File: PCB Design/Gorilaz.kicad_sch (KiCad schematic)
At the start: 44 parts, among them J1 Conn_01x13, J2 Conn_01x13, J3 Conn_01x13, J4 Conn_01x13, J5 Conn_01x13, J6 Conn_01x13, J7 Battery, J8 HRO_TYPE-C-31-M-14, SW1 SW_DPST_x2, SW4 RST, U1 SRV05-4, U10 MAX17048, U3 BQ24075, U4 DW01A, U5 FS8205, U8 nRF52840_moko_mk08

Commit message: up
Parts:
- J7: footprint Local:Molex_Pico-EZmate_78171-0002_1x02-1MP_P1.20mm_Vertical -> Connector_JST:JST_GH_BM02B-GHS-TBT_1x02-1MP_P1.25mm_Vertical
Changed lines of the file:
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@@
 			)
 		)
-		(property "Footprint" "Local:Molex_Pico-EZmate_78171-0002_1x02-1MP_P1.20mm_Vertical"
+		(property "Footprint" "Connector_JST:JST_GH_BM02B-GHS-TBT_1x02-1MP_P1.25mm_Vertical"
 			(at 215.9 52.07 0)
 			(effects

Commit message: update pre-prod
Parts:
- removed SW1: SW_DPST_x2, symbol Switch:SW_DPST_x2
- added JP1: power on, symbol Jumper:SolderJumper_2_Open
- D1, D2, D3: footprint LED_SMD:LED_1206_3216Metric -> LED_SMD:LED_1206_3216Metric_ReverseMount_Hole1.8x2.4mm
- J2: footprint Molex_0039532135 -> Local:Molex_0039532135
- J7: footprint Connector_JST:JST_GH_BM02B-GHS-TBT_1x02-1MP_P1.25mm_Vertical -> Connector_JST:JST_PH_B2B-PH-K_1x02_P2.00mm_Vertical
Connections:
- net +BATT: now also JP1.2 (B)
- net at J7.1 (Pin_1): now also JP1.1 (A)
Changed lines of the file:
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@@
 	(wire
 		(pts
-			(xy 231.14 52.07) (xy 233.68 52.07)
+			(xy 228.6 52.07) (xy 233.68 52.07)
 		)
 		(stroke
@@
 			)
 		)
-		(property "Footprint" "Molex_0039532135"
+		(property "Footprint" "Local:Molex_0039532135"
 			(at 50.8 93.98 0)
 			(effects
@@
 			)
 		)
-		(property "Footprint" "LED_SMD:LED_1206_3216Metric"
+		(property "Footprint" "LED_SMD:LED_1206_3216Metric_ReverseMount_Hole1.8x2.4mm"
 			(at 240.03 180.34 0)
 			(effects
@@
 			)
 		)
-		(property "Footprint" "LED_SMD:LED_1206_3216Metric"
+		(property "Footprint" "LED_SMD:LED_1206_3216Metric_ReverseMount_Hole1.8x2.4mm"
 			(at 281.94 179.07 0)
 			(effects
@@
 	)
 	(symbol
+		(lib_id "Jumper:SolderJumper_2_Open")
+		(at 224.79 52.07 0)
+		(unit 1)
+		(exclude_from_sim no)
+		(in_bom no)
+		(on_board yes)
+		(dnp no)
+		(fields_autoplaced yes)
+		(property "Reference" "JP1"
+			(at 224.79 45.72 0)
+			(effects
+				(font
+					(size 1.27 1.27)
+				)
+			)
+		)
+		(property "Value" "power on"
+			(at 224.79 48.26 0)
+			(effects
+				(font
+					(size 1.27 1.27)
+				)
+			)
+		)
+		(property "Footprint" ""
+			(at 224.79 52.07 0)
+			(effects
+				(font
+					(size 1.27 1.27)
+				)
+				(hide yes)
+			)
+		)
+		(property "Datasheet" "~"
+			(at 224.79 52.07 0)
+			(effects
+				(font
+					(size 1.27 1.27)
+				)
+				(hide yes)
+			)
+		)
+		(property "Description" "Solder Jumper, 2-pole, open"
+			(at 224.79 52.07 0)
+			(effects
+				(font
+					(size 1.27 1.27)
+				)
+				(hide yes)
+			)
+		)
+		(pin "1"
+		)
+		(pin "2"
+		)
+		(instances
+			(project ""
+				(path "/46ef0abf-42df-44ff-8272-0b82956755c4"
+					(reference "JP1")
+					(unit 1)
+				)
+			)
+		)
+	)
+	(symbol
 		(lib_id "power:GND")
 		(at 124.46 66.04 0)
@@
 			)
 		)
-		(property "Footprint" "LED_SMD:LED_1206_3216Metric"
+		(property "Footprint" "LED_SMD:LED_1206_3216Metric_ReverseMount_Hole1.8x2.4mm"
 			(at 269.24 179.07 0)
 			(effects
@@
 	)
 	(symbol
-		(lib_id "Switch:SW_DPST_x2")
-		(at 226.06 52.07 0)
-		(unit 1)
-		(exclude_from_sim no)
-		(in_bom yes)
-		(on_board yes)
-		(dnp no)
-		(fields_autoplaced yes)
-		(property "Reference" "SW1"
-			(at 226.06 45.72 0)
-			(effects
-				(font
-					(size 1.27 1.27)
-				)
-			)
-		)
-		(property "Value" "SW_DPST_x2"
-			(at 226.06 48.26 0)
-			(effects
-				(font
-					(size 1.27 1.27)
-				)
-			)
-		)
-		(property "Footprint" ""
-			(at 226.06 52.07 0)
-			(effects
-				(font
-					(size 1.27 1.27)
-				)
-				(hide yes)
-			)
-		)
-		(property "Datasheet" "~"
-			(at 226.06 52.07 0)
-			(effects
-				(font
-					(size 1.27 1.27)
-				)
-				(hide yes)
-			)
-		)
-		(property "Description" "Single Pole Single Throw (SPST) switch, separate symbol"
-			(at 226.06 52.07 0)
-			(effects
-				(font
-					(size 1.27 1.27)
-				)
-				(hide yes)
-			)
-		)
-		(pin "3"
-		)
-		(pin "2"
-		)
-		(pin "1"
-		)
-		(pin "4"
-		)
-		(instances
-			(project ""
-				(path "/46ef0abf-42df-44ff-8272-0b82956755c4"
-					(reference "SW1")
-					(unit 1)
-				)
-			)
-		)
-	)
-	(symbol
 		(lib_id "power:+BATT")
 		(at 285.75 58.42 0)
@@
 			)
 		)
-		(property "Footprint" "Connector_JST:JST_GH_BM02B-GHS-TBT_1x02-1MP_P1.25mm_Vertical"
+		(property "Footprint" "Connector_JST:JST_PH_B2B-PH-K_1x02_P2.00mm_Vertical"
 			(at 215.9 52.07 0)
 			(effects

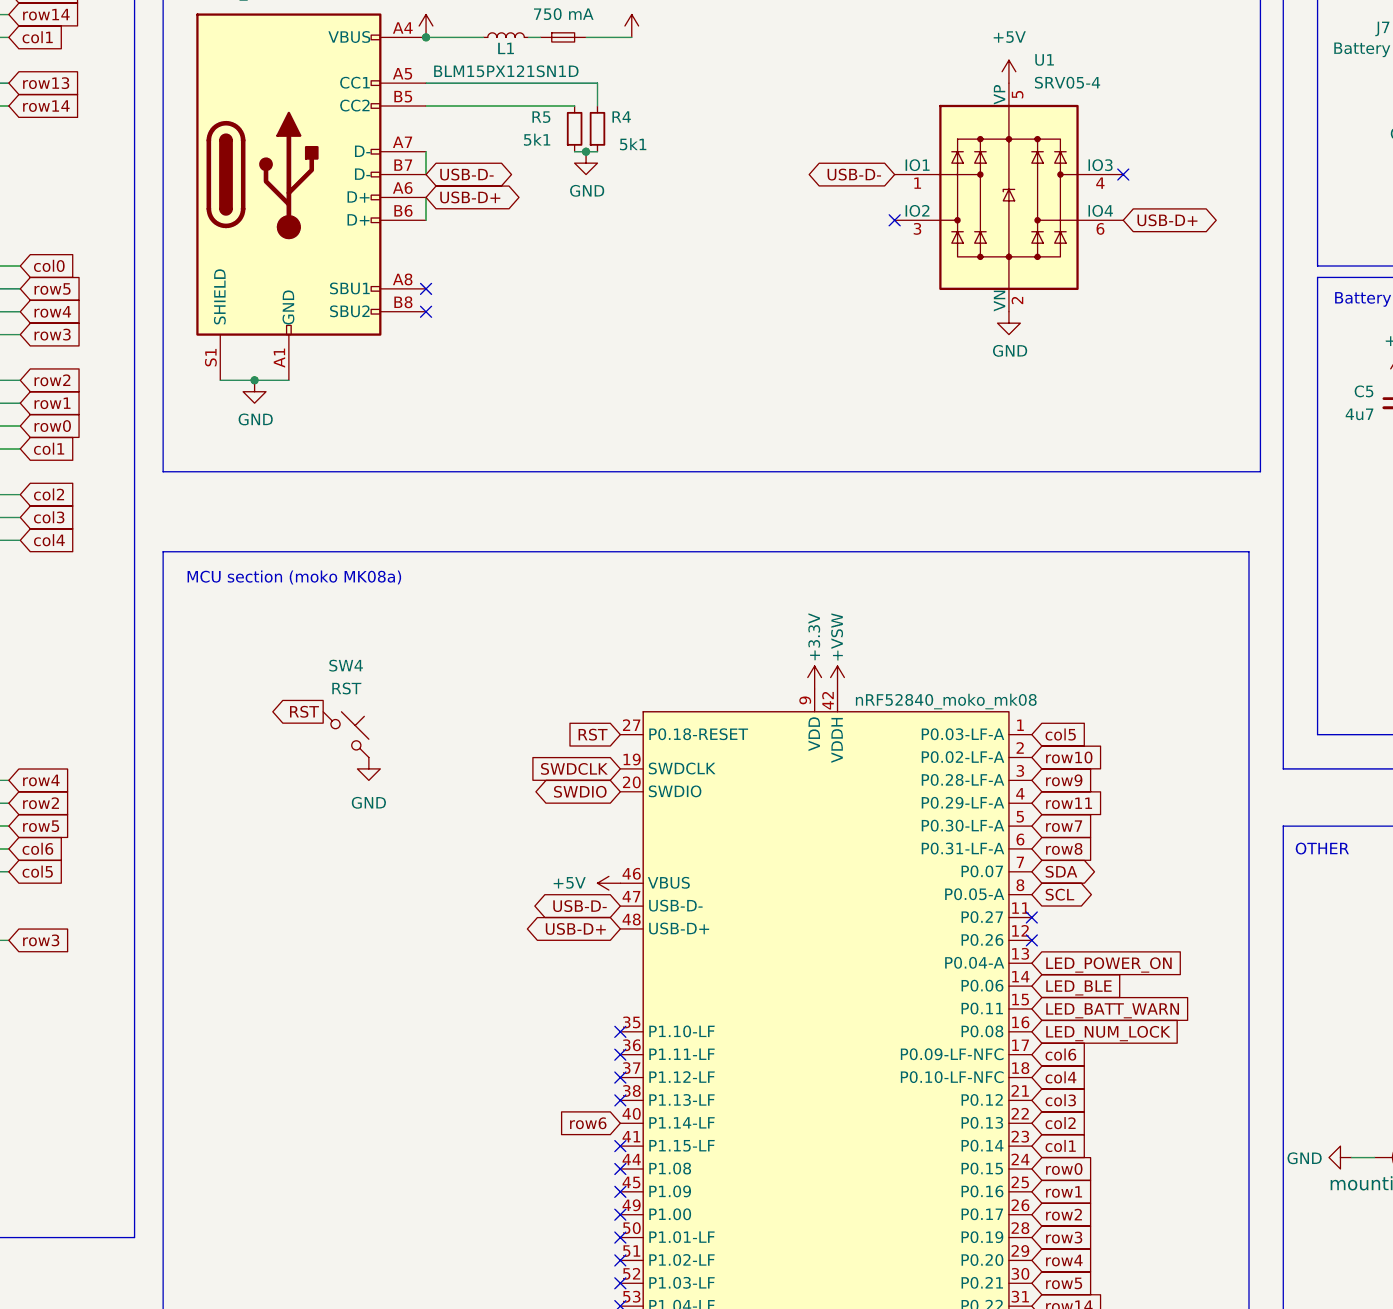
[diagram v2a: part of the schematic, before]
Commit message: ESD update
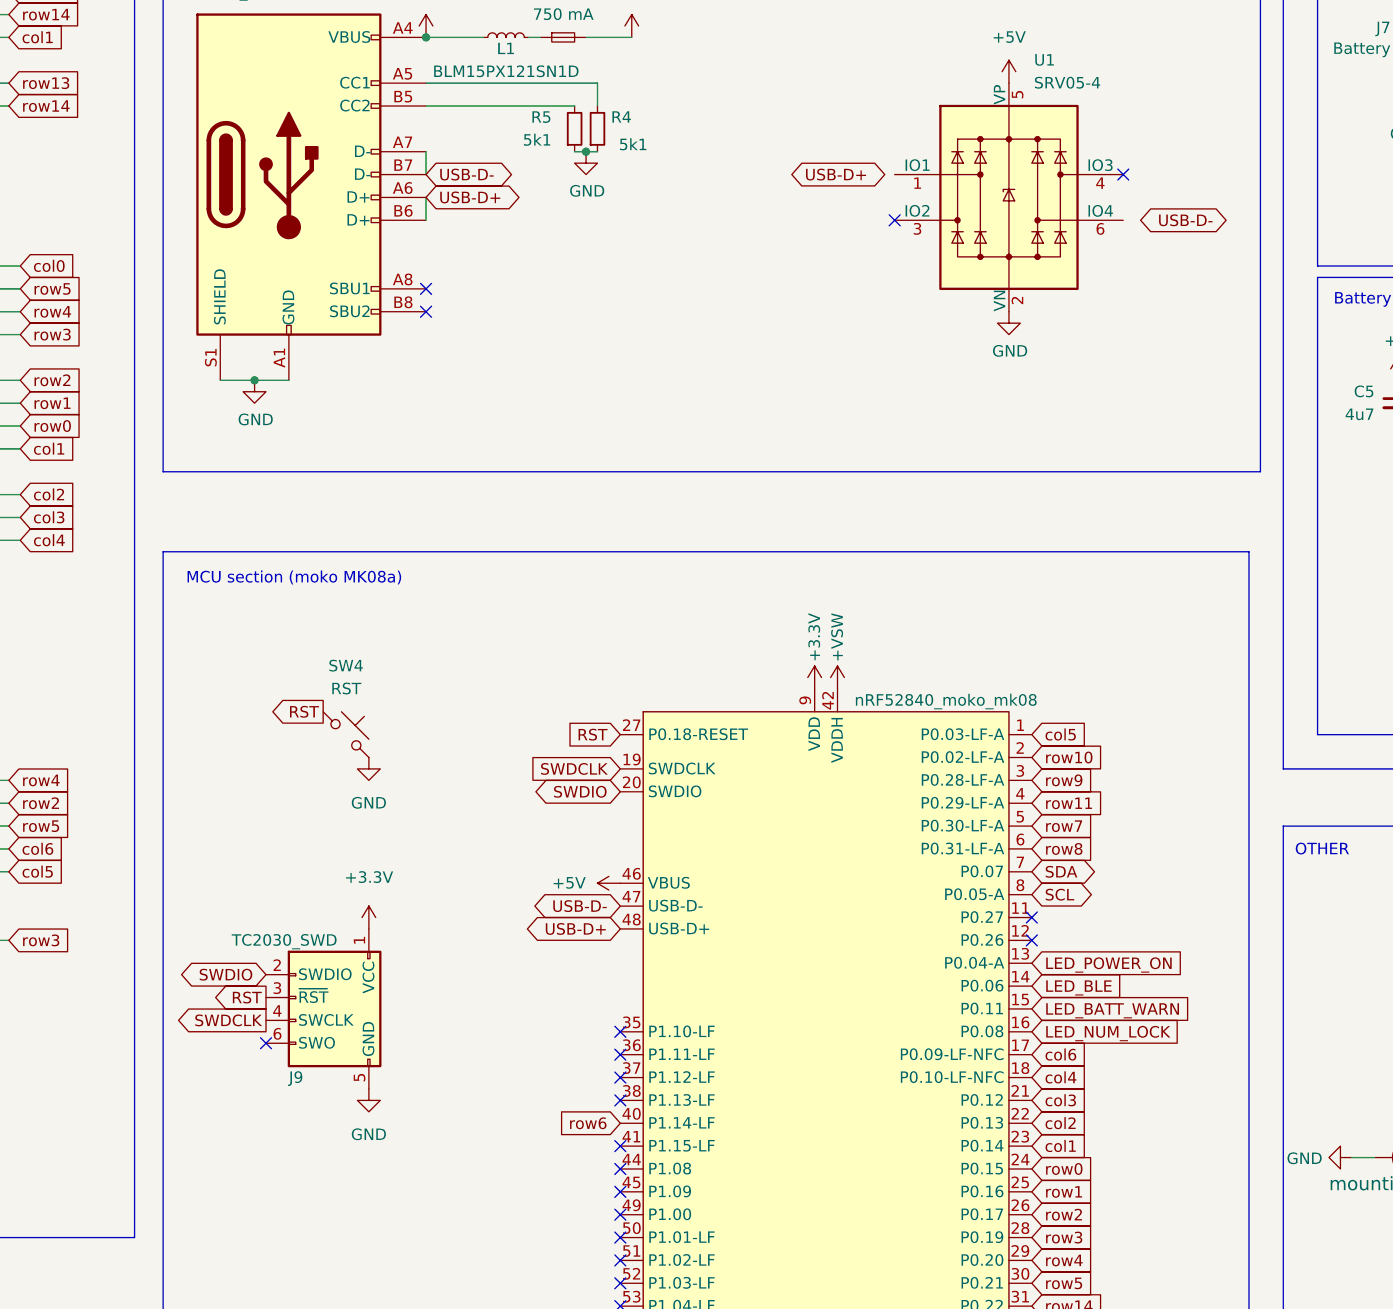
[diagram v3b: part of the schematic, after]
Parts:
- added J9: TC2030_SWD, Mastarlib:CON_TC2030_outlined, symbol PCM_marbastlib-various:TC2030_SWD
- JP1: footprint (none) -> Jumper:SolderJumper-2_P1.3mm_Open_RoundedPad1.0x1.5mm
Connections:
- net +3.3V: now also J9.1 (VCC)
- net GND: now also J9.5 (GND)
- net RST: now also J9.3 (~{RST})
- net SWDCLK: now also J9.4 (SWCLK)
- net SWDIO: now also J9.2 (SWDIO)
- net USB-D+: no longer U1.6 (IO4)
- net USB-D-: no longer U1.1 (IO1)
- no-connect marks 45 -> 46

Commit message: lots of improvement
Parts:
- removed J8: HRO_TYPE-C-31-M-14, Connector_USB:USB_C_Receptacle_HRO_TYPE-C-31-M-12, symbol Connector:USB_C_Receptacle_USB2.0
- removed J9: TC2030_SWD, Mastarlib:CON_TC2030_outlined, symbol PCM_marbastlib-various:TC2030_SWD
- removed JP1: power on, Jumper:SolderJumper-2_P1.3mm_Open_RoundedPad1.0x1.5mm, symbol Jumper:SolderJumper_2_Open
- removed R4, R5: 5k1, Resistor_SMD:R_0402_1005Metric, symbol Device:R_Small
- added C3: 4u7, Capacitor_SMD:C_0402_1005Metric, symbol Device:C_Small
- added CN1: 950-D-SMD-DS/02, easyeda:CONN-SMD_2P-P5.00_950-D-SMD-DS-02, symbol easyea:950-D-SMD-DS_02
- added J8: Conn_01x05_MountingPin, Connector_PinHeader_2.54mm:PinHeader_1x05_P2.54mm_Vertical, symbol Connector_Generic_MountingPin:Conn_01x05_MountingPin
- added R1, R2: 5k1, Resistor_SMD:R_0402_1005Metric, symbol Device:R_Small
- added USB1: USB-310M-B-SU, easyeda:USB-C-SMD_USB-310M-B-SU, symbol easyea:USB-310M-B-SU
- renumbered C8 to C1, C5 to C2, C6 to C4, C17 to C5, LED2 to D1, LED1 to D2, D1 to D3, D2 to D4, D3 to D5, R1 to R10, R2 to R11, R18 to R12, R19 to R13, R20 to R14, R21 to R15, R22 to R16, R15 to R3, R17 to R4, R11 to R5, R12 to R6, R13 to R7, R9 to R8, R10 to R9, SW4 to SW1, U5 to U2, U4 to U3, U3 to U4, U10 to U5
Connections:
- net +3.3V: now also J8.1 (Pin_1)
- net +BATT: now also C3.1, CN1.2
- net ALERT: now also U8.54 (P1.05-LF)
- net GND: now also C3.2, J8.5 (Pin_5), J8.MP (MountPin), R1.1, R2.1, USB1.1 (SHELL), USB1.2 (SHELL), USB1.3 (SHELL), USB1.4 (SHELL), USB1.A1B12 (GND), USB1.B1A12 (GND)
- net RST: now also J8.3 (Pin_3)
- net SWDCLK: now also J8.4 (Pin_4)
- net SWDIO: now also J8.2 (Pin_2)
- net USB-D+: now also USB1.A6 (DP1), USB1.B6 (DP2)
- net USB-D-: now also USB1.A7 (DN1), USB1.B7 (DN2)
- net VBUS: now also USB1.B4A9 (VBUS)
- net col0: now also U8.34 (P0.25); no longer U8.33 (P0.24)
- net col1: now also U8.29 (P0.20); no longer U8.23 (P0.14)
- net col2: now also U8.30 (P0.21); no longer U8.22 (P0.13)
- net row0: now also U8.22 (P0.13); no longer U8.24 (P0.15)
- net row1: now also U8.23 (P0.14); no longer U8.25 (P0.16)
- net row12: now also U8.33 (P0.24); no longer U8.34 (P0.25)
- net row2: now also U8.24 (P0.15); no longer U8.26 (P0.17)
- net row3: now also U8.25 (P0.16); no longer U8.28 (P0.19)
- net row4: now also U8.26 (P0.17); no longer U8.29 (P0.20)
- net row5: now also U8.28 (P0.19); no longer U8.30 (P0.21)
- net at J7.1 (Pin_1): now also CN1.1
- new net: R2.2, USB1.B5 (CC2)
- new net: R1.2, USB1.A5 (CC1)
- no-connect marks 46 -> 45
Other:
- moved on the sheet: U1

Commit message: clean up
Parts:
- J8: footprint Connector_PinHeader_2.54mm:PinHeader_1x05_P2.54mm_Vertical -> Connector_PinHeader_2.54mm:PinHeader_1x05_P2.54mm_Vertical_SMD_Pin1Left
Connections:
- net LED_BATT_WARN: now also R14.2, U8.13 (P0.04-A); no longer R16.2, U8.15 (P0.11)
- net LED_POWER_ON: now also R16.2, U8.15 (P0.11); no longer R14.2, U8.13 (P0.04-A)
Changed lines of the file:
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@@
 		)
 	)
-	(global_label "LED_POWER_ON"
-		(shape input)
-		(at 173.99 156.21 0)
-		(fields_autoplaced yes)
-		(effects
-			(font
-				(size 1.27 1.27)
-			)
-			(justify left)
-		)
-		(property "Intersheetrefs" "${INTERSHEET_REFS}"
-			(at 191.4894 156.21 0)
-			(effects
-				(font
-					(size 1.27 1.27)
-				)
-				(justify left)
-				(hide yes)
-			)
-		)
-	)
 	(global_label "row6"
 		(shape input)
@@
 		)
 	)
-	(global_label "LED_BATT_WARN"
-		(shape input)
-		(at 173.99 161.29 0)
-		(fields_autoplaced yes)
-		(effects
-			(font
-				(size 1.27 1.27)
-			)
-			(justify left)
-		)
-		(property "Intersheetrefs" "${INTERSHEET_REFS}"
-			(at 191.7918 161.29 0)
-			(effects
-				(font
-					(size 1.27 1.27)
-				)
-				(justify left)
-				(hide yes)
-			)
-		)
-	)
 	(global_label "col6"
 		(shape input)
@@
 		)
 	)
-	(global_label "LED_BLE"
-		(shape input)
-		(at 173.99 158.75 0)
-		(fields_autoplaced yes)
-		(effects
-			(font
-				(size 1.27 1.27)
-			)
-			(justify left)
-		)
-		(property "Intersheetrefs" "${INTERSHEET_REFS}"
-			(at 184.837 158.75 0)
-			(effects
-				(font
-					(size 1.27 1.27)
-				)
-				(justify left)
-				(hide yes)
-			)
-		)
-	)
-	(global_label "LED_BATT_WARN"
-		(shape input)
-		(at 281.94 167.64 90)
-		(fields_autoplaced yes)
-		(effects
-			(font
-				(size 1.27 1.27)
-			)
-			(justify left)
-		)
-		(property "Intersheetrefs" "${INTERSHEET_REFS}"
-			(at 281.94 149.8382 90)
-			(effects
-				(font
-					(size 1.27 1.27)
-				)
-				(justify left)
-				(hide yes)
-			)
-		)
-	)
 	(global_label "row13"
 		(shape input)
@@
 		)
 	)
+	(global_label "LED_POWER_ON"
+		(shape input)
+		(at 173.99 161.29 0)
+		(fields_autoplaced yes)
+		(effects
+			(font
+				(size 1.27 1.27)
+			)
+			(justify left)
+		)
+		(property "Intersheetrefs" "${INTERSHEET_REFS}"
+			(at 191.4894 161.29 0)
+			(effects
+				(font
+					(size 1.27 1.27)
+				)
+				(justify left)
+				(hide yes)
+			)
+		)
+	)
 	(global_label "col3"
 		(shape input)
@@
 		)
 	)
+	(global_label "LED_BATT_WARN"
+		(shape input)
+		(at 173.99 156.21 0)
+		(fields_autoplaced yes)
+		(effects
+			(font
+				(size 1.27 1.27)
+			)
+			(justify left)
+		)
+		(property "Intersheetrefs" "${INTERSHEET_REFS}"
+			(at 191.7918 156.21 0)
+			(effects
+				(font
+					(size 1.27 1.27)
+				)
+				(justify left)
+				(hide yes)
+			)
+		)
+	)
 	(global_label "row8"
 		(shape input)
@@
 		)
 	)
+	(global_label "LED_POWER_ON"
+		(shape input)
+		(at 281.94 167.64 90)
+		(fields_autoplaced yes)
+		(effects
+			(font
+				(size 1.27 1.27)
+			)
+			(justify left)
+		)
+		(property "Intersheetrefs" "${INTERSHEET_REFS}"
+			(at 281.94 150.1406 90)
+			(effects
+				(font
+					(size 1.27 1.27)
+				)
+				(justify left)
+				(hide yes)
+			)
+		)
+	)
 	(global_label "row2"
 		(shape input)
@@
 		)
 	)
+	(global_label "LED_BLE"
+		(shape input)
+		(at 173.99 158.75 0)
+		(fields_autoplaced yes)
+		(effects
+			(font
+				(size 1.27 1.27)
+			)
+			(justify left)
+		)
+		(property "Intersheetrefs" "${INTERSHEET_REFS}"
+			(at 184.837 158.75 0)
+			(effects
+				(font
+					(size 1.27 1.27)
+				)
+				(justify left)
+				(hide yes)
+			)
+		)
+	)
 	(global_label "col3"
 		(shape input)
@@
 		)
 	)
-	(global_label "LED_POWER_ON"
-		(shape input)
-		(at 240.03 168.91 90)
-		(fields_autoplaced yes)
-		(effects
-			(font
-				(size 1.27 1.27)
-			)
-			(justify left)
-		)
-		(property "Intersheetrefs" "${INTERSHEET_REFS}"
-			(at 240.03 151.4106 90)
-			(effects
-				(font
-					(size 1.27 1.27)
-				)
-				(justify left)
-				(hide yes)
-			)
-		)
-	)
 	(global_label "ALERT"
 		(shape input)
@@
 		)
 	)
+	(global_label "LED_BATT_WARN"
+		(shape input)
+		(at 240.03 168.91 90)
+		(fields_autoplaced yes)
+		(effects
+			(font
+				(size 1.27 1.27)
+			)
+			(justify left)
+		)
+		(property "Intersheetrefs" "${INTERSHEET_REFS}"
+			(at 240.03 151.1082 90)
+			(effects
+				(font
+					(size 1.27 1.27)
+				)
+				(justify left)
+				(hide yes)
+			)
+		)
+	)
 	(global_label "row14"
 		(shape input)
@@
 			)
 		)
-		(property "Description" ""
+		(property "Description" "C15464"
 			(at 243.84 106.68 0)
 			(effects
@@
 			)
 		)
-		(property "Footprint" "Connector_PinHeader_2.54mm:PinHeader_1x05_P2.54mm_Vertical"
+		(property "Footprint" "Connector_PinHeader_2.54mm:PinHeader_1x05_P2.54mm_Vertical_SMD_Pin1Left"
 			(at 97.79 165.1 0)
 			(effects
@@
 			)
 		)
-		(property "Description" ""
+		(property "Description" "C2682616"
 			(at 298.45 64.77 0)
 			(effects

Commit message: LED update
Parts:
- D1: renamed from D5; value LED_SCR -> LED_PWON
- D3: value LED_CAPS -> LED_BATT_WARN
- D4: renamed from D1; footprint LED_SMD:LED_0402_1005Metric -> LED_SMD:LED_1206_3216Metric_ReverseMount_Hole1.8x2.4mm
- D5: renamed from D4; value LED_NUM -> LED_BLE
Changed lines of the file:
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@@
 			)
 		)
-		(property "Value" "LED_CAPS"
+		(property "Value" "LED_BATT_WARN"
 			(at 243.0272 181.6862 90)
 			(effects
@@
 		(on_board yes)
 		(dnp no)
-		(property "Reference" "D5"
+		(property "Reference" "D1"
 			(at 284.9372 178.1048 90)
 			(effects
@@
 			)
 		)
-		(property "Value" "LED_SCR"
+		(property "Value" "LED_PWON"
 			(at 284.9372 180.4162 90)
 			(effects
@@
 			(project "Gorilaz"
 				(path "/46ef0abf-42df-44ff-8272-0b82956755c4"
-					(reference "D5")
+					(reference "D1")
 					(unit 1)
 				)
@@
 		(on_board yes)
 		(dnp no)
-		(property "Reference" "D4"
+		(property "Reference" "D5"
 			(at 272.2372 178.1048 90)
 			(effects
@@
 			)
 		)
-		(property "Value" "LED_NUM"
+		(property "Value" "LED_BLE"
 			(at 272.2372 180.4162 90)
 			(effects
@@
 			(project "Gorilaz"
 				(path "/46ef0abf-42df-44ff-8272-0b82956755c4"
-					(reference "D4")
+					(reference "D5")
 					(unit 1)
 				)
@@
 		(on_board yes)
 		(dnp no)
-		(property "Reference" "D1"
+		(property "Reference" "D4"
 			(at 273.05 99.06 90)
 			(effects
@@
 			)
 		)
-		(property "Footprint" "LED_SMD:LED_0402_1005Metric"
+		(property "Footprint" "LED_SMD:LED_1206_3216Metric_ReverseMount_Hole1.8x2.4mm"
 			(at 280.67 100.33 90)
 			(effects
@@
 			(project "Gorilaz"
 				(path "/46ef0abf-42df-44ff-8272-0b82956755c4"
-					(reference "D1")
-					(unit 1)
-				)
+					(reference "D4")
+					(unit 1)
+				)
